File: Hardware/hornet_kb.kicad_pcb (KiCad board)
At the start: 2 copper layers, 90 parts, among them J1 Conn_ST_STDC14, J10 USB_C_Receptacle_USB2.0, SW1 ESC, SW10 TAB, SW11 Q, SW12 W, SW13 E, SW14 R, SW15 T, SW17 M1, SW18 CAPS, SW19 A, SW2 `, SW20 S, SW21 D, SW22 F, SW23 G, SW25 M2, SW26 M3, SW28 SHIFT, SW29 CTRL, SW3 1, SW31 Z, SW32 WIN, SW34 X, SW35 FN, SW37 C, SW38 ALT, SW4 2, SW40 V, SW41 SPACE, SW43 B, SW44 DEL, SW5 3, SW6 4, SW7 5, SW8 6, SW9 M0, U1 nRF52840, U2 BQ24040, U3 BQ51050BRHL, U4 AP22814BW5

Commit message: Completed keymatrix layout
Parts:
- added C10: 820pF, Capacitor_SMD:C_0603_1608Metric, F.Cu at (272.7, 132.0)
- added C12: 4.7uF, Capacitor_SMD:C_0805_2012Metric, F.Cu at (282.0, 130.7)
- added C13: 200nF, Capacitor_SMD:C_0603_1608Metric, F.Cu at (272.7, 102.4)
- added C14: 22nF, Capacitor_SMD:C_0603_1608Metric, F.Cu at (272.7, 104.9)
- added C15: 10nF, Capacitor_SMD:C_0603_1608Metric, F.Cu at (272.7, 107.4)
- added C16: 470pF, Capacitor_SMD:C_0603_1608Metric, F.Cu at (272.7, 109.9)
- added C17: 2.2nF, Capacitor_SMD:C_0603_1608Metric, F.Cu at (272.7, 112.4)
- added C18: 470pF, Capacitor_SMD:C_0603_1608Metric, F.Cu at (272.7, 114.9)
- added C19: 22nF, Capacitor_SMD:C_0603_1608Metric, F.Cu at (272.7, 117.5)
- added C20: 10nF, Capacitor_SMD:C_0603_1608Metric, F.Cu at (272.7, 120.0)
- added C22: 10uF, Capacitor_SMD:C_0603_1608Metric, F.Cu at (276.7, 102.4)
- added C23: 1uF, Capacitor_SMD:C_0603_1608Metric, F.Cu at (276.7, 104.9)
- added C24: 10uF, Capacitor_SMD:C_0603_1608Metric, F.Cu at (276.7, 107.4)
- added C25: 10uF, Capacitor_SMD:C_0603_1608Metric, F.Cu at (276.7, 109.9)
- added C26: 10uF, Capacitor_SMD:C_0603_1608Metric, F.Cu at (276.7, 112.4)
- added C27: 20uF, Capacitor_SMD:C_0603_1608Metric, F.Cu at (276.7, 114.9)
- added C28: 1pF, Capacitor_SMD:C_0402_1005Metric, F.Cu at (276.2, 133.9)
- added C29: 1pF, Capacitor_SMD:C_0402_1005Metric, F.Cu at (276.2, 135.9)
- added C5: 4.7uF, Capacitor_SMD:C_0805_2012Metric, F.Cu at (282.0, 127.7)
- added C6: 100pF, Capacitor_SMD:C_0603_1608Metric, F.Cu at (272.7, 124.5)
- added C7: 100nF, Capacitor_SMD:C_0603_1608Metric, F.Cu at (272.7, 127.0)
- added C9: 1uF, Capacitor_SMD:C_0603_1608Metric, F.Cu at (272.7, 129.5)
- added D97: USB_CHG, LED_SMD:LED_0402_1005Metric, F.Cu at (284.4, 120.0)
- added J2: Conn_01x03, Connector_JST:JST_GH_SM02B-GHS-TB_1x02-1MP_P1.25mm_Horizontal, F.Cu at (230.1, 101.7)
- added L1: 6.3uH, Connector_JST:JST_EH_S2B-EH_1x02_P2.50mm_Horizontal, F.Cu at (227.2, 81.8)
- added L5: 4.7nH, Inductor_SMD:L_0402_1005Metric, F.Cu at (281.2, 133.2)
- added NT1: NetTie_2, NetTie:NetTie-2_SMD_Pad2.0mm, F.Cu at (278.2, 124.7)
- added R1: 500, Resistor_SMD:R_0603_1608Metric, F.Cu at (276.7, 117.5)
- added R10: 200, Resistor_SMD:R_0603_1608Metric, F.Cu at (280.7, 114.9)
- added R11: 10k, Resistor_SMD:R_0603_1608Metric, F.Cu at (280.7, 117.5)
- added R12: 10k, Resistor_SMD:R_0603_1608Metric, F.Cu at (272.7, 134.5)
- added R13: 0, Resistor_SMD:R_0402_1005Metric, F.Cu at (281.2, 135.2)
- added R2: 1k, Resistor_SMD:R_0603_1608Metric, F.Cu at (276.7, 120.0)
- added R4: 2k, Resistor_SMD:R_0603_1608Metric, F.Cu at (280.7, 102.4)
- added R5: 10k, Resistor_SMD:R_0603_1608Metric, F.Cu at (280.7, 104.9)
- added R6: 500, Resistor_SMD:R_0603_1608Metric, F.Cu at (280.7, 107.4)
- added R8: 2.4k, Resistor_SMD:R_0603_1608Metric, F.Cu at (280.7, 109.9)
- added R9: 400, Resistor_SMD:R_0603_1608Metric, F.Cu at (280.7, 112.4)
- added Y1: 32.768kHz, Crystal:Crystal_SMD_3215-2Pin_3.2x1.5mm, F.Cu at (277.3, 127.9)
- added Y2: 32MHz, Crystal:Crystal_SMD_3215-2Pin_3.2x1.5mm, F.Cu at (277.3, 131.2)
- D1, D10, D11, D12, D13, D14, D15, D17, D18, D19, D2, D20, D21, D22, D23, D25, D26, D28, D29, D3, D31, D32, D34, D35, D37, D38, D4, D40, D41, D43, D44, D5, D6, D7, D8, D9: moved to B.Cu
- moved J1 48.1 mm to (280.2, 72.6)
- moved U1 40.5 mm to (205.8, 76.7)
- moved D8 0.32 mm to (195.8, 64.2)
- moved D7 0.10 mm to (175.8, 64.3)
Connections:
- U1 pad AD16: unconnected-(U1-P0.20-PadAD16) -> R_COL_7
- U2 pad 5: Net-(D98-K) -> unconnected-(U2-~{PG}-Pad5)
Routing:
- net R_ROW_4: track 0.00 -> 155.5 mm
- net R_ROW_3: track 0.00 -> 146.5 mm, vias 0 -> 10
- net R_ROW_2: track 0.00 -> 130.4 mm, vias 0 -> 12
- net R_ROW_1: track 0.00 -> 125.6 mm, vias 0 -> 12
- net R_ROW_0: track 0.00 -> 114.9 mm, vias 0 -> 12
- net R_COL_2: track 0.00 -> 101.7 mm
- net R_COL_3: track 0.00 -> 93.0 mm
- net R_COL_6: track 0.00 -> 92.0 mm
- net R_COL_4: track 0.00 -> 91.0 mm
- net R_COL_5: track 0.00 -> 87.5 mm
- net R_COL_1: track 0.00 -> 85.7 mm
- net R_COL_0: track 0.00 -> 76.2 mm
- net Net-(D41-A): track 0.00 -> 19.0 mm
- net Net-(D28-A): track 0.00 -> 18.8 mm
- net Net-(D18-A): track 0.00 -> 14.6 mm
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
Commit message: Added LDO to battery and added placement for the charging modules
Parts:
- added C11: 1uF, Capacitor_SMD:C_0603_1608Metric, F.Cu at (240.5, 70.1)
- added C8: 1uF, Capacitor_SMD:C_0603_1608Metric, F.Cu at (240.5, 67.6)
- added U5: AP7333, Package_TO_SOT_SMD:SOT-23, F.Cu at (223.7, 63.3)
- J2, JP1, JP3: moved to B.Cu
- moved R1 92.7 mm to (214.5, 48.7)
- moved R2 91.5 mm to (213.5, 53.8)
- moved D97 91.1 mm to (226.4, 49.8)
- moved C27 88.5 mm to (207.3, 60.0), turned to 90 degrees
- moved Y2 87.4 mm to (201.7, 87.2)
- moved C20 87.0 mm to (209.6, 60.0), turned to -90 degrees
- moved R11 86.9 mm to (215.5, 60.0), turned to -90 degrees
- moved Y1 86.8 mm to (207.9, 75.6), turned to 135 degrees
- moved J1 84.9 mm to (199.8, 99.7), turned to 180 degrees
- moved R7 83.6 mm to (201.5, 56.1), turned to 0 degrees
- moved C17 83.2 mm to (205.0, 64.1), turned to 90 degrees
- moved C19 82.5 mm to (213.4, 60.0), turned to -90 degrees
- moved C18 82.3 mm to (211.4, 60.0), turned to -90 degrees
- moved R24 82.0 mm to (200.5, 54.0), turned to 0 degrees
- moved R23 80.5 mm to (205.9, 54.0)
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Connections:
- C26 pad 1: VDD1 -> VDD
- J1 pad 3: VDD1 -> VDD
- U1 pad A22: VDD1 -> VDD
- U1 pad AD14: VDD1 -> VDD
- U1 pad AD23: VDD1 -> VDD
- U1 pad B1: VDD1 -> VDD
- U1 pad W1: VDD1 -> VDD
- U1 pad Y2: VDD1 -> VDD
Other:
- board outline added: 195.1 x 100.9 mm
- board text added: "This board will be a double sided assembly, due to the indication LEDs needed on the top and the hotswap sockets on the bottom."
- board text removed: "For the sake of price and challenge (mainly price...), This design will be a SINGLE sided assembly with all parts mounted on the REAR end of the board alongside the hotswap sockets"

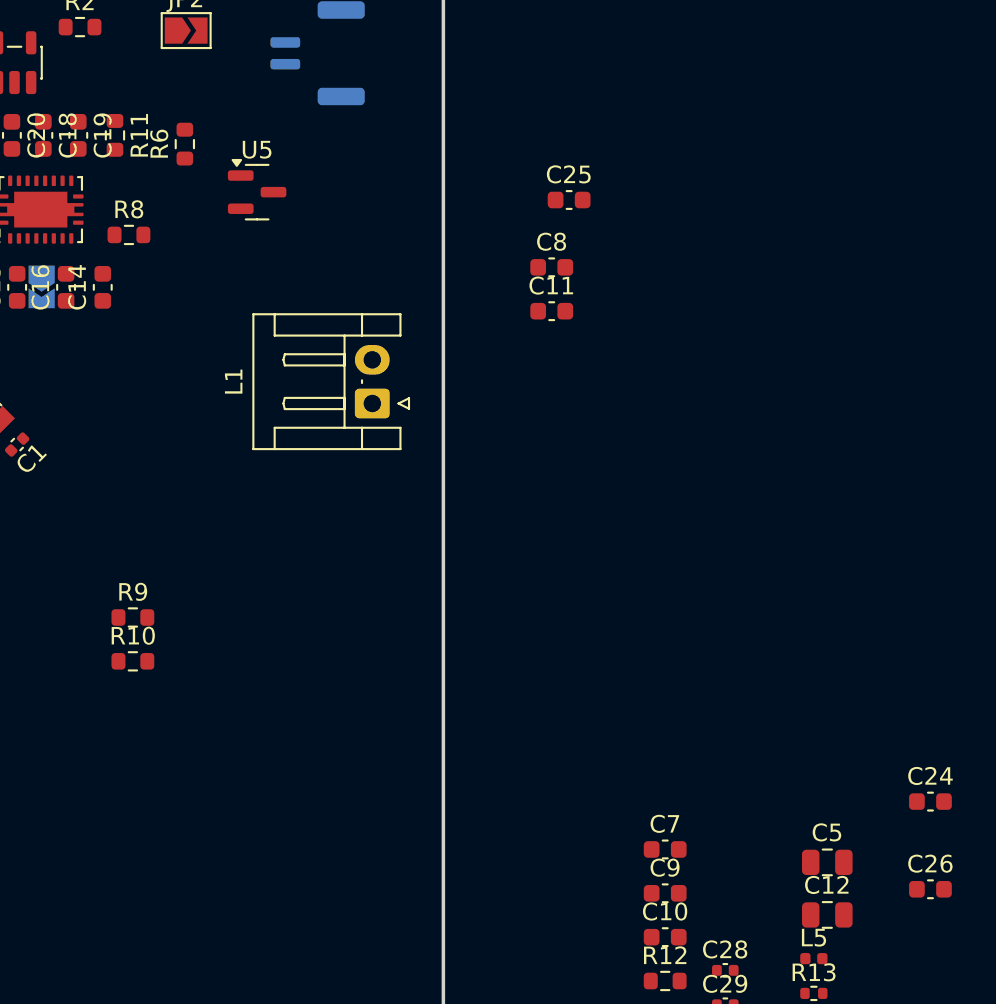
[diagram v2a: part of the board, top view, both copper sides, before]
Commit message: Update PCB net names
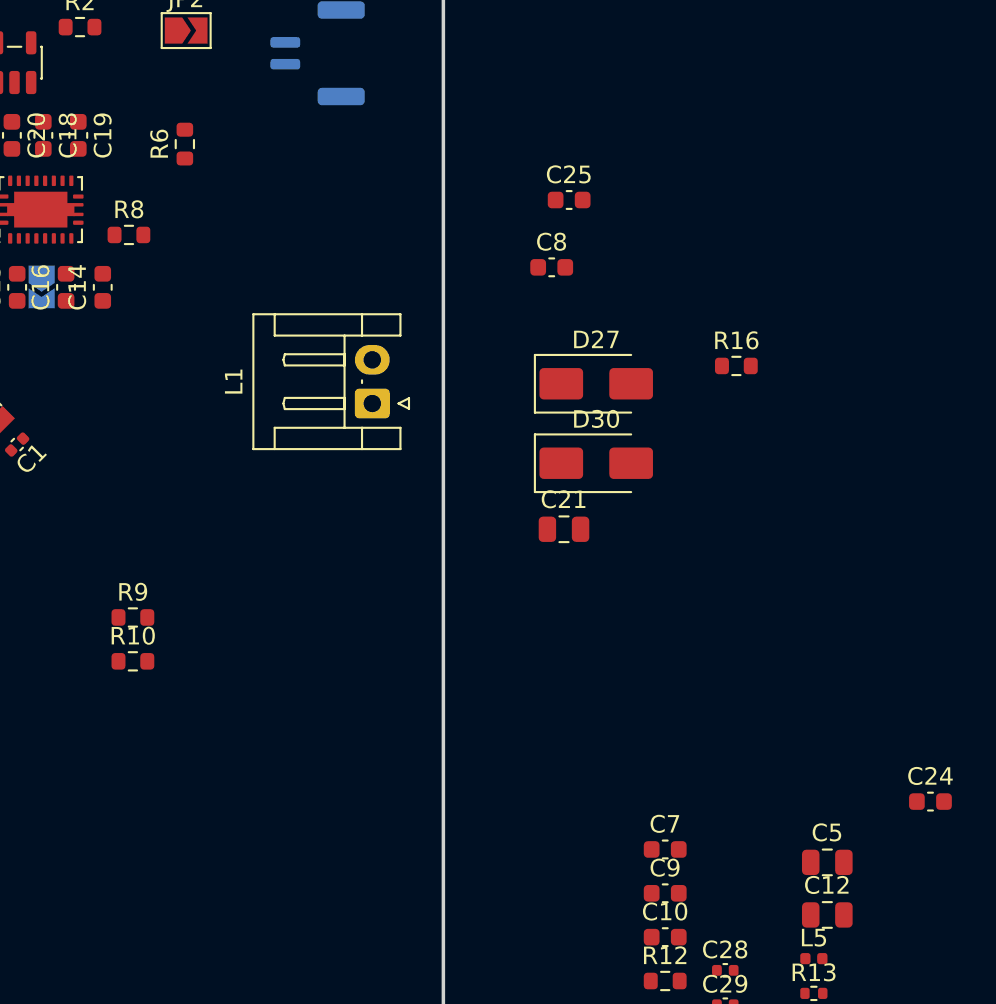
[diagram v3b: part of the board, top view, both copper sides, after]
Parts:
- removed C11: 1uF, Capacitor_SMD:C_0603_1608Metric
- removed C26: 10uF, Capacitor_SMD:C_0603_1608Metric
- removed R11: 10k, Resistor_SMD:R_0603_1608Metric
- removed U5: AP7333, Package_TO_SOT_SMD:SOT-23
- added C21: 4.7uF, Capacitor_SMD:C_0805_2012Metric, F.Cu at (241.2, 82.6)
- added D27: SS14, Diode_SMD:D_SMA, F.Cu at (243.1, 74.2)
- added D30: SS14, Diode_SMD:D_SMA, F.Cu at (243.1, 78.8)
- added R16: 200, Resistor_SMD:R_0603_1608Metric, F.Cu at (251.1, 73.2)
- C27: value 20uF -> 4.7uF
- C8: value 1uF -> 100pF
- JP1: value USB_CHG_ENA1 -> BATTERY_ENA
- R9: value 400 -> 10k
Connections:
- net R_COL_0 renamed /R_COL_0
- net R_COL_1 renamed /R_COL_1
- net R_COL_2 renamed /R_COL_2
- net R_COL_3 renamed /R_COL_3
- net R_COL_4 renamed /R_COL_4
- net R_COL_5 renamed /R_COL_5
- net R_COL_6 renamed /R_COL_6
- net R_COL_7 renamed /R_COL_7
- net R_ROW_0 renamed /R_ROW_0
- net R_ROW_3 renamed /R_ROW_3
- net R_ROW_4 renamed /R_ROW_4
- C1 pad 1: GND1 -> GND
- C10 pad 1: GND1 -> GND
- C12 pad 2: GND1 -> GND
- C2 pad 1: GND1 -> GND
- C22 pad 2: GND1 -> GND
- C23 pad 1: GND1 -> GND
- C23 pad 2: Net-(JP1-B) -> Net-(U2-IN)
- C24 pad 2: GND1 -> GND
- C25 pad 1: GND1 -> GND
- C27 pad 2: GND1 -> GND
- C29 pad 2: GND1 -> GND
- C5 pad 1: GND1 -> VBUS
- C5 pad 2: VBUS -> GND
- C6 pad 2: GND1 -> GND
- C7 pad 2: GND1 -> GND
- C8 pad 1: GND1 -> Net-(U3-AC2)
- C8 pad 2: Net-(SW27A-C) -> Net-(U3-AC1)
- C9 pad 2: GND1 -> GND
- D10 pad 1: R_ROW_1 -> /R_ROW_2
- D11 pad 1: R_ROW_1 -> /R_ROW_2
- D12 pad 1: R_ROW_1 -> /R_ROW_2
- D13 pad 1: R_ROW_1 -> /R_ROW_2
- D14 pad 1: R_ROW_1 -> /R_ROW_2
- D15 pad 1: R_ROW_1 -> /R_ROW_2
- D17 pad 1: R_ROW_2 -> /R_ROW_1
- D18 pad 1: R_ROW_2 -> /R_ROW_1
- D19 pad 1: R_ROW_2 -> /R_ROW_1
- D20 pad 1: R_ROW_2 -> /R_ROW_1
- D21 pad 1: R_ROW_2 -> /R_ROW_1
- D22 pad 1: R_ROW_2 -> /R_ROW_1
- D23 pad 1: R_ROW_2 -> /R_ROW_1
- D9 pad 1: R_ROW_1 -> /R_ROW_2
- J1 pad 11: GND1 -> GND
- J1 pad 5: GND1 -> GND
- J1 pad 7: GND1 -> GND
- J2 pad 2: GND1 -> GND
- JP1 pad 2: Net-(JP1-B) -> +VDC
- NT1 pad 2: GND1 -> GND
- R10 pad 2: GND1 -> GND
- R12 pad 1: VDD1 -> VDD
- R2 pad 1: GND1 -> GND
- R4 pad 1: GND1 -> GND
- R7 pad 1: VDD1 -> VDD
- R8 pad 2: GND1 -> GND
- R9 pad 1: Net-(U3-RECT) -> VDD
- R9 pad 2: Net-(U3-ILIM) -> Net-(U3-TS/CTRL)
- U1 pad B7: GND1 -> GND
- U1 pad EP: GND1 -> GND
- U1 pad P2: unconnected-(U1-P1.08-PadP2) -> /Rotary_L
- U1 pad P23: unconnected-(U1-P1.07-PadP23) -> /Rotary_R
- U1 pad R1: unconnected-(U1-TRACEDATA3/P1.09-PadR1) -> /Rotary_SW
- U1 pad R24: R_ROW_5 -> unconnected-(U1-P1.06-PadR24)
- U1 pad V23: R_ROW_2 -> /R_ROW_2
- U1 pad W24: R_ROW_1 -> /R_ROW_1
- U1 pad Y2: VDD -> Net-(D27-K)
- U2 pad 1: Net-(JP1-B) -> Net-(U2-IN)
- U2 pad 3: GND1 -> GND
- U2 pad 7: GND1 -> GND
- U3 pad 1: GND1 -> GND
- U3 pad 11: GND1 -> GND
- U3 pad 20: GND1 -> GND
- U3 pad 21: GND1 -> GND
- U4 pad 1: Net-(JP1-A) -> Net-(U2-IN)
- U4 pad 2: GND1 -> GND
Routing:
- net R_ROW_2: track 130.4 -> 0.00 mm, vias 12 -> 0
- net /R_ROW_1: track 0.00 -> 130.4 mm, vias 0 -> 12
- net R_ROW_1: track 125.6 -> 0.00 mm, vias 12 -> 0
- net /R_ROW_2: track 0.00 -> 125.6 mm, vias 0 -> 12

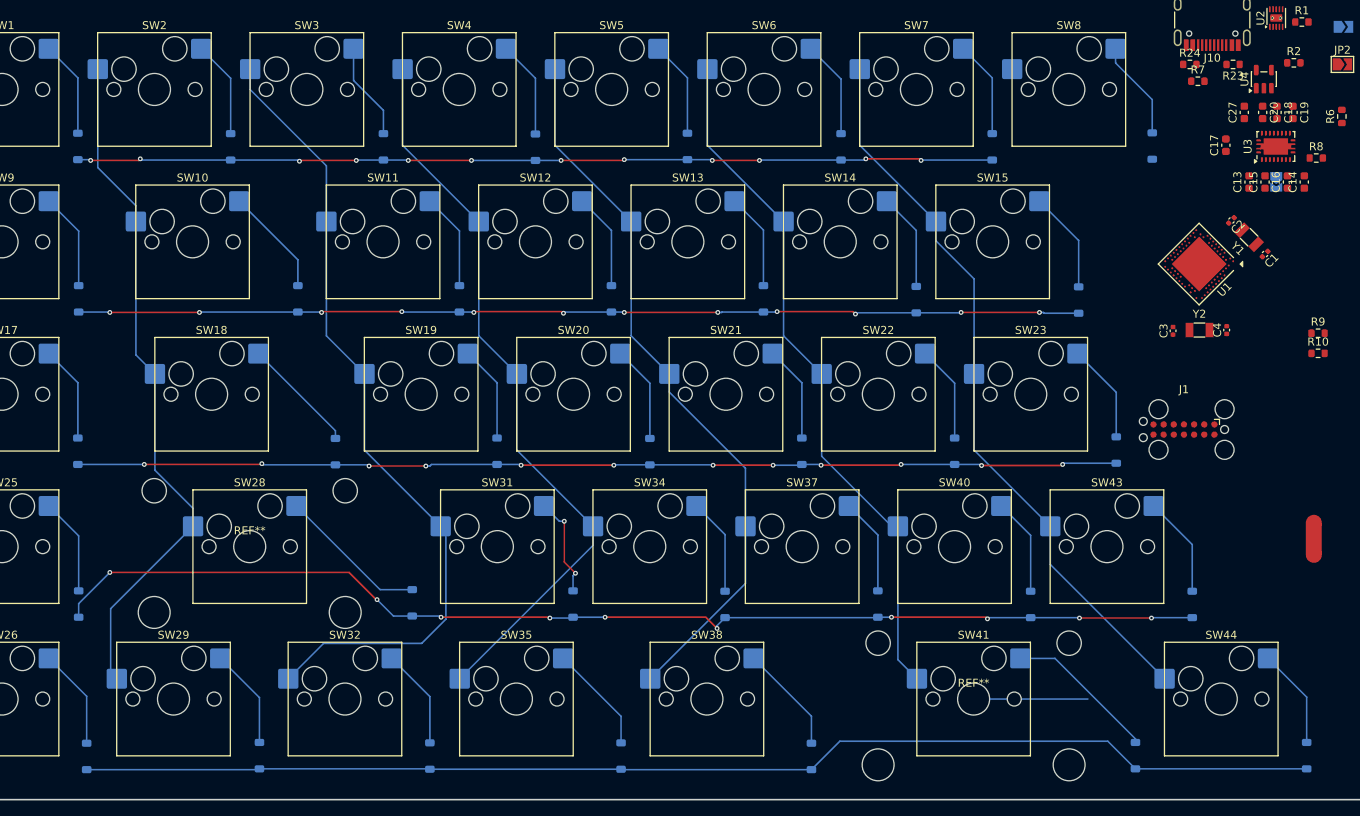
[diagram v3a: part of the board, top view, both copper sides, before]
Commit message: Route dual sided hotswap/diodes assmebly
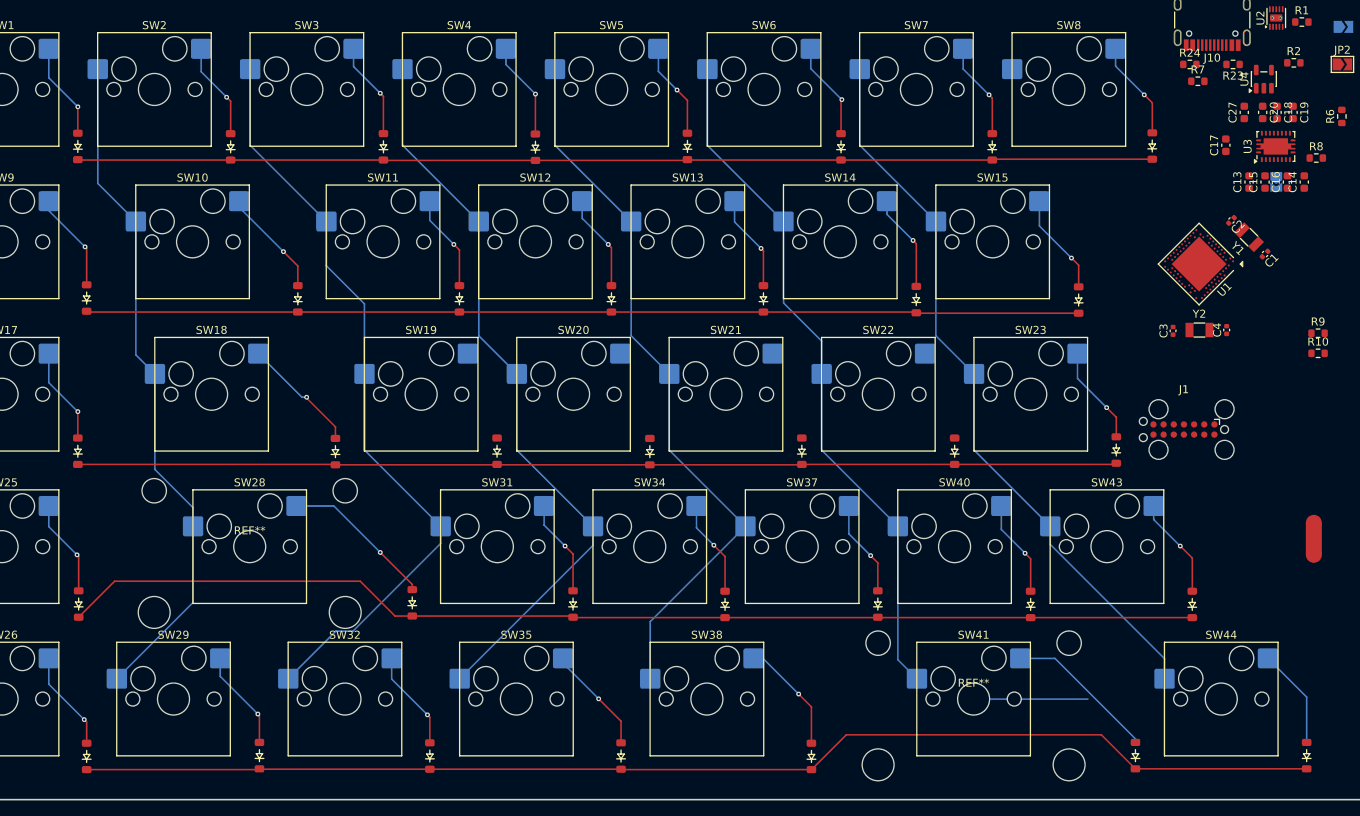
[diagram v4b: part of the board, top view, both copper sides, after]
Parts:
- D1, D10, D11, D12, D13, D14, D15, D17, D18, D19, D2, D20, D21, D22, D23, D25, D26, D28, D29, D3, D31, D32, D34, D35, D37, D38, D4, D40, D41, D43, D44, D5, D6, D7, D8, D9: moved to F.Cu
- moved D9 1.00 mm to (62.6, 83.2)
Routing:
- net /R_ROW_0: track 114.9 -> 134.4 mm, vias 12 -> 0
- net Net-(D20-A): track 12.1 -> 0.00 mm
- net Net-(D22-A): track 12.1 -> 0.00 mm
- net Net-(D21-A): track 12.1 -> 0.00 mm
- net Net-(D19-A): track 12.1 -> 0.00 mm
- net /R_ROW_3: track 146.5 -> 143.0 mm, vias 10 -> 0
- net /R_COL_2: track 101.7 -> 104.7 mm
- net /R_ROW_2: track 125.6 -> 124.1 mm, vias 12 -> 0
- net Net-(D38-A): track 13.6 -> 14.3 mm, vias 0 -> 1
- net /R_ROW_4: track 155.5 -> 156.1 mm
- net /R_COL_1: track 85.7 -> 85.1 mm
- net Net-(D31-A): track 12.7 -> 12.1 mm, vias 2 -> 1
- net /R_ROW_1: track 130.4 -> 129.9 mm, vias 12 -> 0
- net Net-(D28-A): track 18.8 -> 19.2 mm, vias 0 -> 1
- net Net-(D18-A): track 14.6 -> 14.9 mm, vias 0 -> 1
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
